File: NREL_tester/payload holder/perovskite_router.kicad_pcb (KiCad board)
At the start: 2 copper layers, 45.1 x 38.4 mm, 3 parts, among them J1 Conn_01x10_Male, J2 Conn_01x10_Male, J3 Conn_01x11_Male

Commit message: Flight computer v2 complete
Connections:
- J3 pad 10: SCL -> GND
- J3 pad 11: SDA -> COMMON_1
- J3 pad 8: GND -> SDA
- J3 pad 9: COMMON_1 -> SCL
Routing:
- net GND: track 38.7 -> 23.0 mm
- net COMMON_1: track 51.0 -> 60.3 mm
- net SDA: track 30.1 -> 25.1 mm
- net SCL: track 25.1 -> 24.6 mm

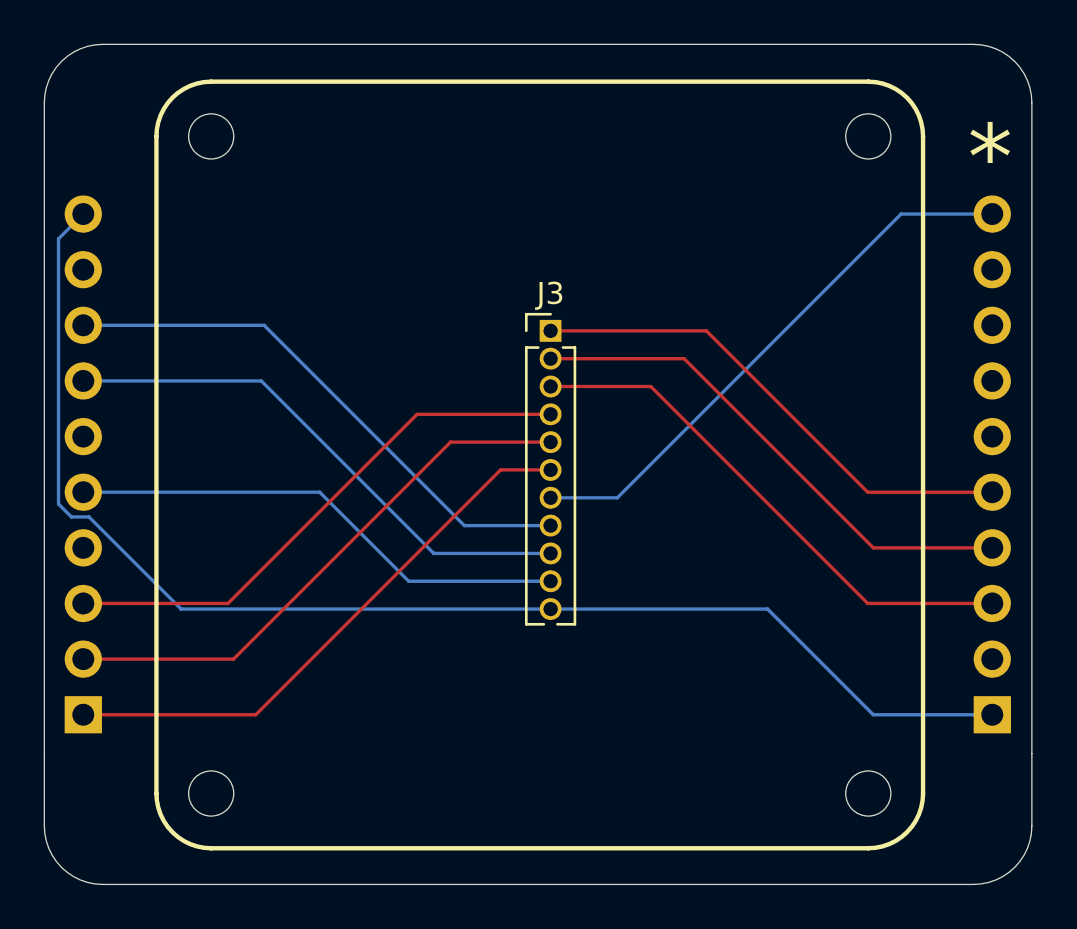
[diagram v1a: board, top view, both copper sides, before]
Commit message: Update hardware
- Add separate discharge resistance paths to flight computer
- Update footprint for payload holder
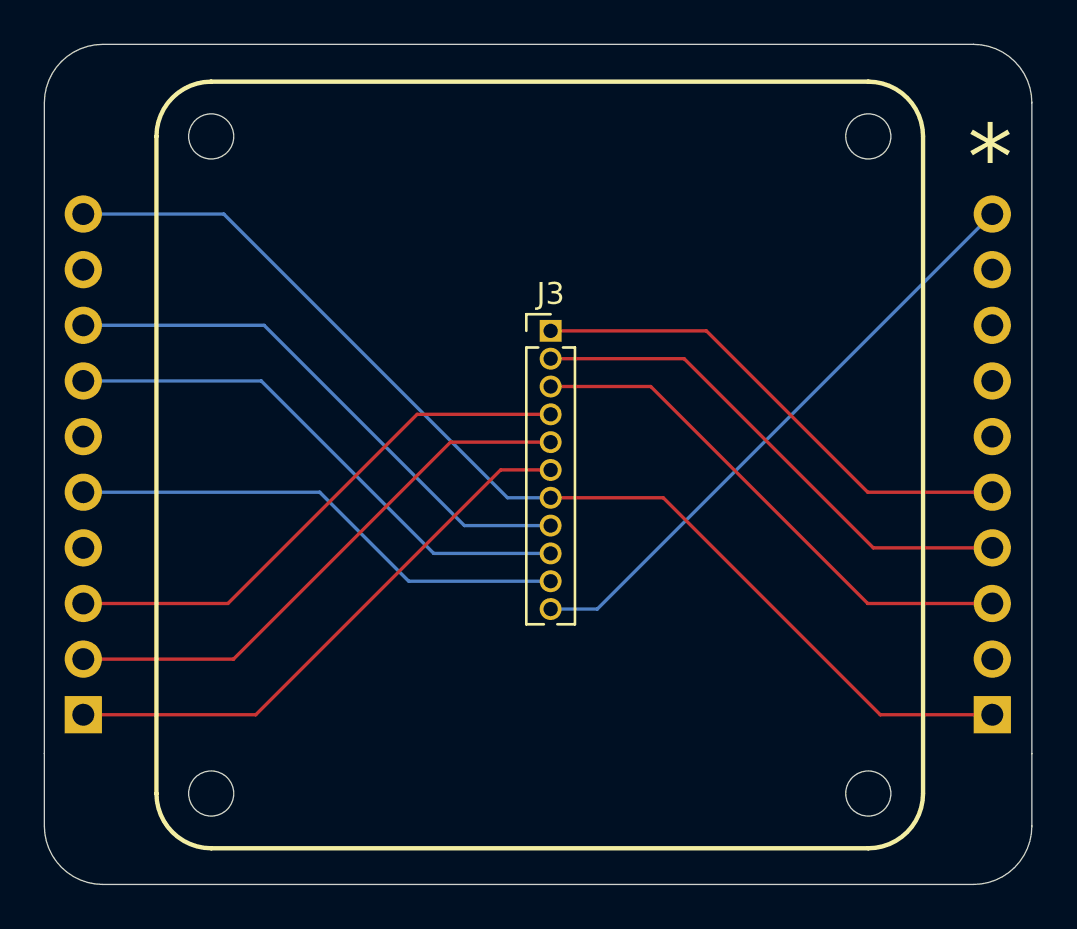
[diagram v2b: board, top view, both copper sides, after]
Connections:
- J3 pad 11: COMMON_1 -> +3V3
- J3 pad 7: +3V3 -> COMMON_1
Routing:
- net COMMON_1: track 60.3 -> 51.0 mm
- net +3V3: track 25.5 -> 27.6 mm
